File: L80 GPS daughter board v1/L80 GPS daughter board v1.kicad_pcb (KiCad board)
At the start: 2 copper layers, 29.8 x 18 mm, 12 parts, among them J1 Conn_01x06_Socket, U1 AP2112K-3.3, U2 L80-R, U3 MCP73831-2-OT

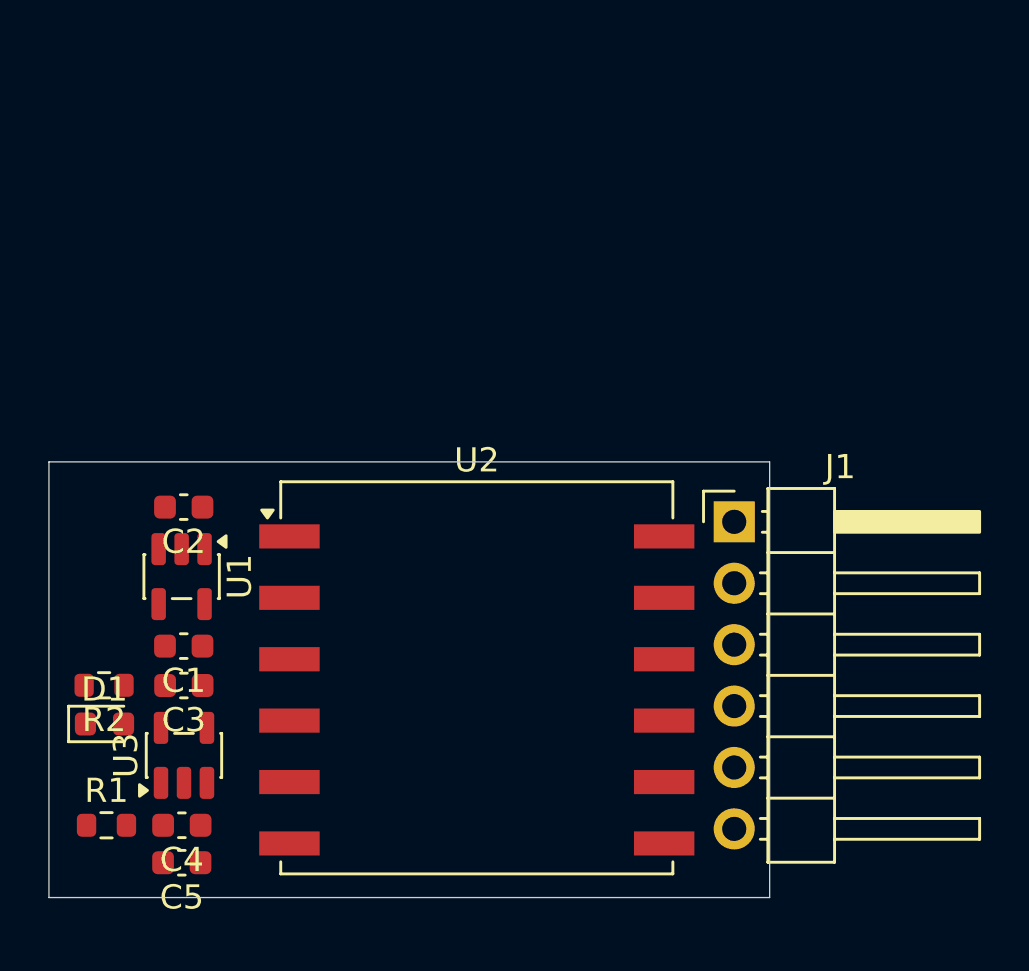
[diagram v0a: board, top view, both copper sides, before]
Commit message: started working on the L80 GPS carrier board
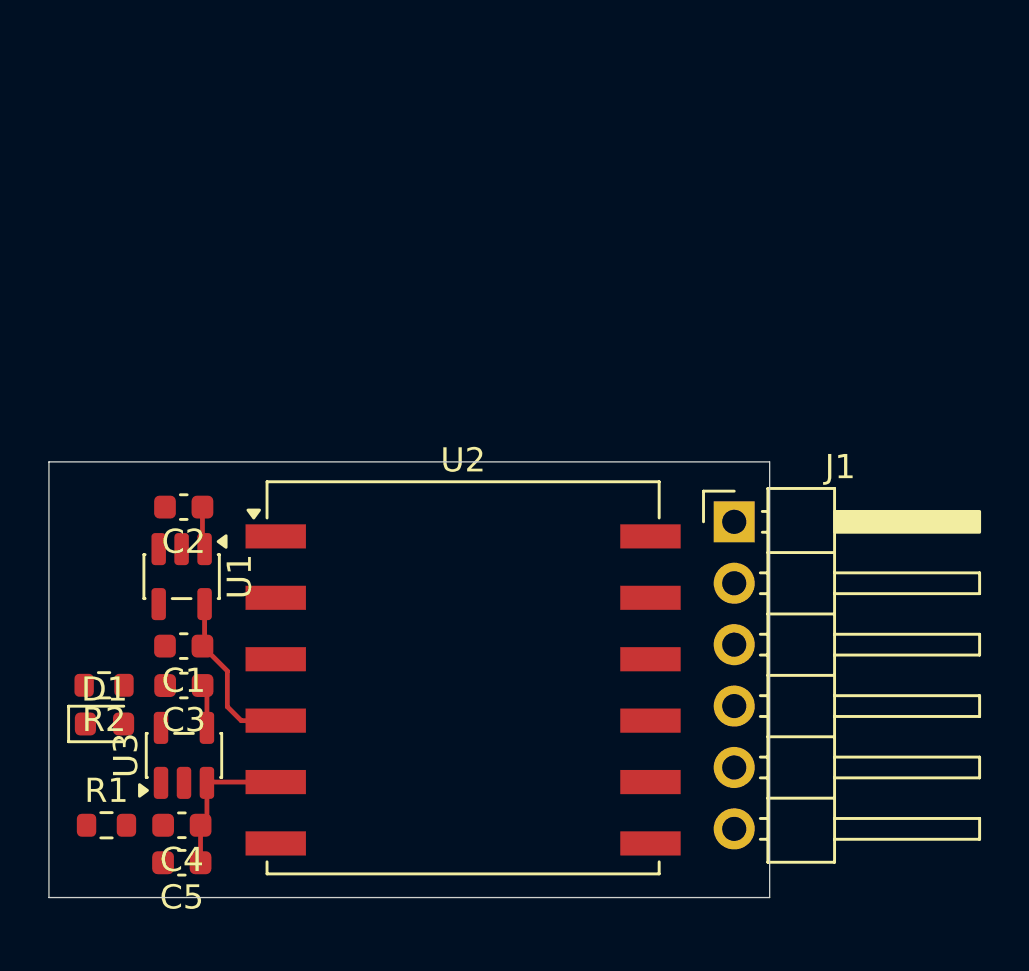
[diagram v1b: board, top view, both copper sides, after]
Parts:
- moved U2 0.57 mm to (134.2, 106.8)
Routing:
- net GPS_PWR: track 0.00 -> 6.95 mm
- net VBAT_RTC: track 0.00 -> 6.27 mm
- net +5V: track 0.00 -> 3.60 mm
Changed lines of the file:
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@@
 	(footprint "RF_GPS:Quectel_L80-R"
 		(layer "F.Cu")
-		(at 134.817089 106.801883)
+		(at 134.25 106.801883)
 		(descr "Quectel L80-R GPS Module, Patch on Top, https://www.quectel.com/UploadImage/Downlad/Quectel_L80-R_Hardware_Design_V1.2.pdf")
 		(tags "quectel GPS GNSS")
@@
 			(polygon
 				(pts
-					(xy 135.471864 106.171883) (xy 135.452801 105.953994) (xy 135.396192 105.742725) (xy 135.303756 105.544496)
-					(xy 135.178302 105.365329) (xy 135.023643 105.21067) (xy 134.844477 105.085216) (xy 134.646247 104.99278)
-					(xy 134.434978 104.936171) (xy 134.217089 104.917108) (xy 133.9992 104.936171) (xy 133.787931 104.99278)
-					(xy 133.589702 105.085216) (xy 133.410535 105.21067) (xy 133.255876 105.365329) (xy 133.130422 105.544496)
-					(xy 133.037986 105.742725) (xy 132.981377 105.953994) (xy 132.962314 106.171883) (xy 132.981377 106.389772)
-					(xy 133.037986 106.601041) (xy 133.130422 106.79927) (xy 133.255876 106.978437) (xy 133.410535 107.133096)
-					(xy 133.589701 107.25855) (xy 133.787931 107.350986) (xy 133.9992 107.407595) (xy 134.217089 107.426658)
-					(xy 134.434978 107.407595) (xy 134.646247 107.350986) (xy 134.844477 107.25855) (xy 135.023643 107.133096)
-					(xy 135.178302 106.978437) (xy 135.303756 106.79927) (xy 135.396192 106.601041) (xy 135.452801 106.389772)
+					(xy 134.904775 106.171883) (xy 134.885712 105.953994) (xy 134.829103 105.742725) (xy 134.736667 105.544496)
+					(xy 134.611213 105.365329) (xy 134.456554 105.21067) (xy 134.277388 105.085216) (xy 134.079158 104.99278)
+					(xy 133.867889 104.936171) (xy 133.65 104.917108) (xy 133.432111 104.936171) (xy 133.220842 104.99278)
+					(xy 133.022613 105.085216) (xy 132.843446 105.21067) (xy 132.688787 105.365329) (xy 132.563333 105.544496)
+					(xy 132.470897 105.742725) (xy 132.414288 105.953994) (xy 132.395225 106.171883) (xy 132.414288 106.389772)
+					(xy 132.470897 106.601041) (xy 132.563333 106.79927) (xy 132.688787 106.978437) (xy 132.843446 107.133096)
+					(xy 133.022612 107.25855) (xy 133.220842 107.350986) (xy 133.432111 107.407595) (xy 133.65 107.426658)
+					(xy 133.867889 107.407595) (xy 134.079158 107.350986) (xy 134.277388 107.25855) (xy 134.456554 107.133096)
+					(xy 134.611213 106.978437) (xy 134.736667 106.79927) (xy 134.829103 106.601041) (xy 134.885712 106.389772)
 				)
 			)
@@
 		(layer "Edge.Cuts")
 	)
+	(segment
+		(start 123.5575 105.4025)
+		(end 123.47 105.49)
+		(width 0.2)
+		(layer "F.Cu")
+		(net 2)
+	)
+	(segment
+		(start 126.5 108.571883)
+		(end 125.071883 108.571883)
+		(width 0.2)
+		(layer "F.Cu")
+		(net 2)
+	)
+	(segment
+		(start 125.071883 108.571883)
+		(end 124.5 108)
+		(width 0.2)
+		(layer "F.Cu")
+		(net 2)
+	)
+	(segment
+		(start 123.5575 103.7525)
+		(end 123.5575 105.4025)
+		(width 0.2)
+		(layer "F.Cu")
+		(net 2)
+	)
+	(segment
+		(start 124.5 106.52)
+		(end 124.5 108)
+		(width 0.2)
+		(layer "F.Cu")
+		(net 2)
+	)
+	(segment
+		(start 123.47 105.49)
+		(end 124.5 106.52)
+		(width 0.2)
+		(layer "F.Cu")
+		(net 2)
+	)
+	(segment
+		(start 123.655 107.3)
+		(end 123.475 107.12)
+		(width 0.2)
+		(layer "F.Cu")
+		(net 3)
+	)
+	(segment
+		(start 123.47 101.39)
+		(end 123.5575 101.4775)
+		(width 0.2)
+		(layer "F.Cu")
+		(net 3)
+	)
+	(segment
+		(start 123.655 108.8725)
+		(end 123.655 107.3)
+		(width 0.2)
+		(layer "F.Cu")
+		(net 3)
+	)
+	(segment
+		(start 123.47 99.74)
+		(end 123.47 101.39)
+		(width 0.2)
+		(layer "F.Cu")
+		(net 3)
+	)
+	(segment
+		(start 123.655 111.1475)
+		(end 123.655 112.6375)
+		(width 0.2)
+		(layer "F.Cu")
+		(net 14)
+	)
+	(segment
+		(start 123.39 112.9025)
+		(end 123.3925 112.9)
+		(width 0.2)
+		(layer "F.Cu")
+		(net 14)
+	)
+	(segment
+		(start 123.39 114.45)
+		(end 123.39 112.9025)
+		(width 0.2)
+		(layer "F.Cu")
+		(net 14)
+	)
+	(segment
+		(start 123.655 112.6375)
+		(end 123.3925 112.9)
+		(width 0.2)
+		(layer "F.Cu")
+		(net 14)
+	)
+	(segment
+		(start 123.690617 111.111883)
+		(end 123.655 111.1475)
+		(width 0.2)
+		(layer "F.Cu")
+		(net 14)
+	)
+	(segment
+		(start 126.5 111.111883)
+		(end 123.690617 111.111883)
+		(width 0.2)
+		(layer "F.Cu")
+		(net 14)
+	)
 	(embedded_fonts no)

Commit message: routed the l80 gps daughter board and a few more modifications
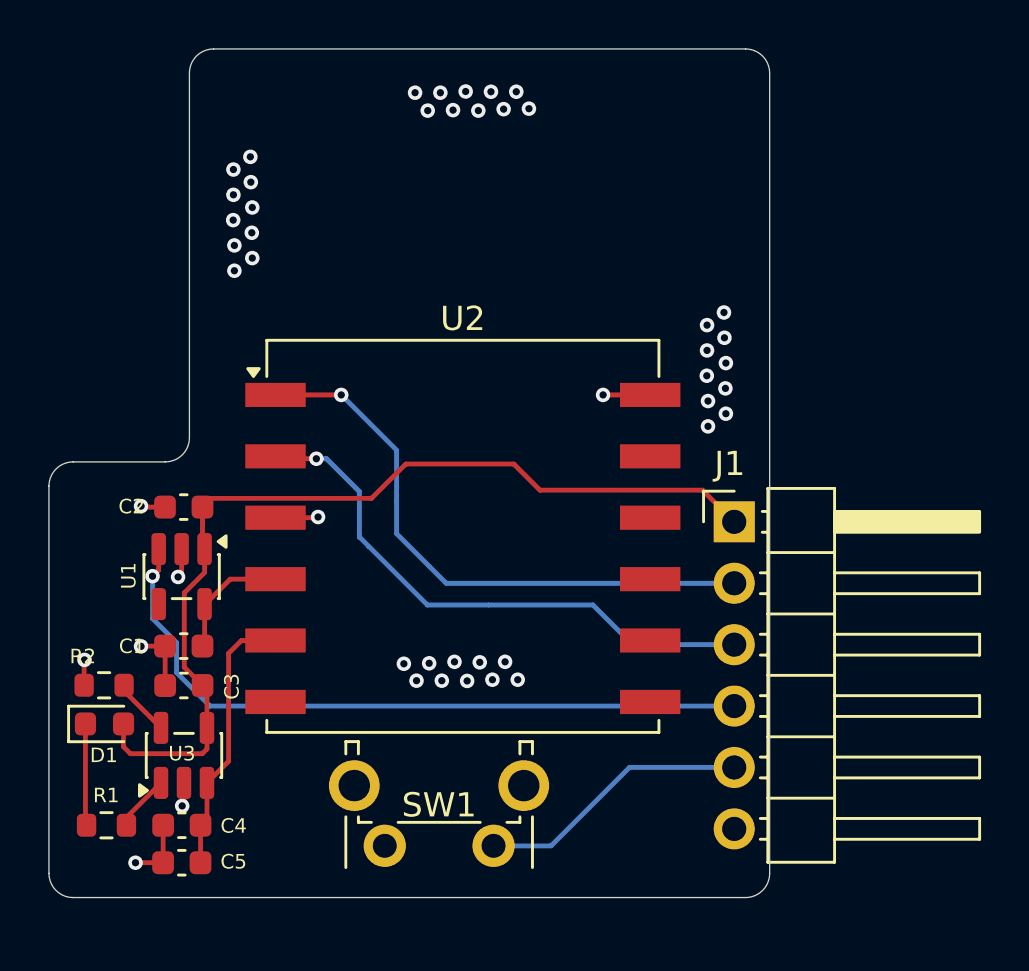
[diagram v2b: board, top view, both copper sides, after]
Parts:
- added SW1: SW_Push, Button_Switch_THT:SW_Tactile_SPST_Angled_PTS645Vx39-2LFS, F.Cu at (135.5, 113.8)
- moved U2 5.85 mm to (134.2, 101.0)
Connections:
- J1 pad 5: unconnected-(J1-Pin_5-Pad5) -> PWR_SWITCH
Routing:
- net +5V: track 3.60 -> 39.1 mm
- net GPS_Switch: track 0.00 -> 29.3 mm, vias 0 -> 1
- net gps_rx: track 0.00 -> 24.2 mm, vias 0 -> 1
- net gps_tx: track 0.00 -> 23.3 mm, vias 0 -> 1
- net GND: track 0.00 -> 13.3 mm, vias 0 -> 48
- net PWR_SWITCH: track 0.00 -> 11.3 mm
- net VBAT_RTC: track 6.27 -> 11.3 mm
- net Net-(D1-K): track 0.00 -> 4.21 mm
- net Net-(U3-PROG): track 0.00 -> 2.40 mm
- net stat: track 0.00 -> 2.34 mm
- net GPS_PWR: track 6.95 -> 5.13 mm
- added copper zone on In1.Cu, net GND
- added copper zone on In2.Cu, net GND
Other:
- board size 29.8 x 18 mm -> 29.8 x 35.1 mm
- copper layers 2 -> 4

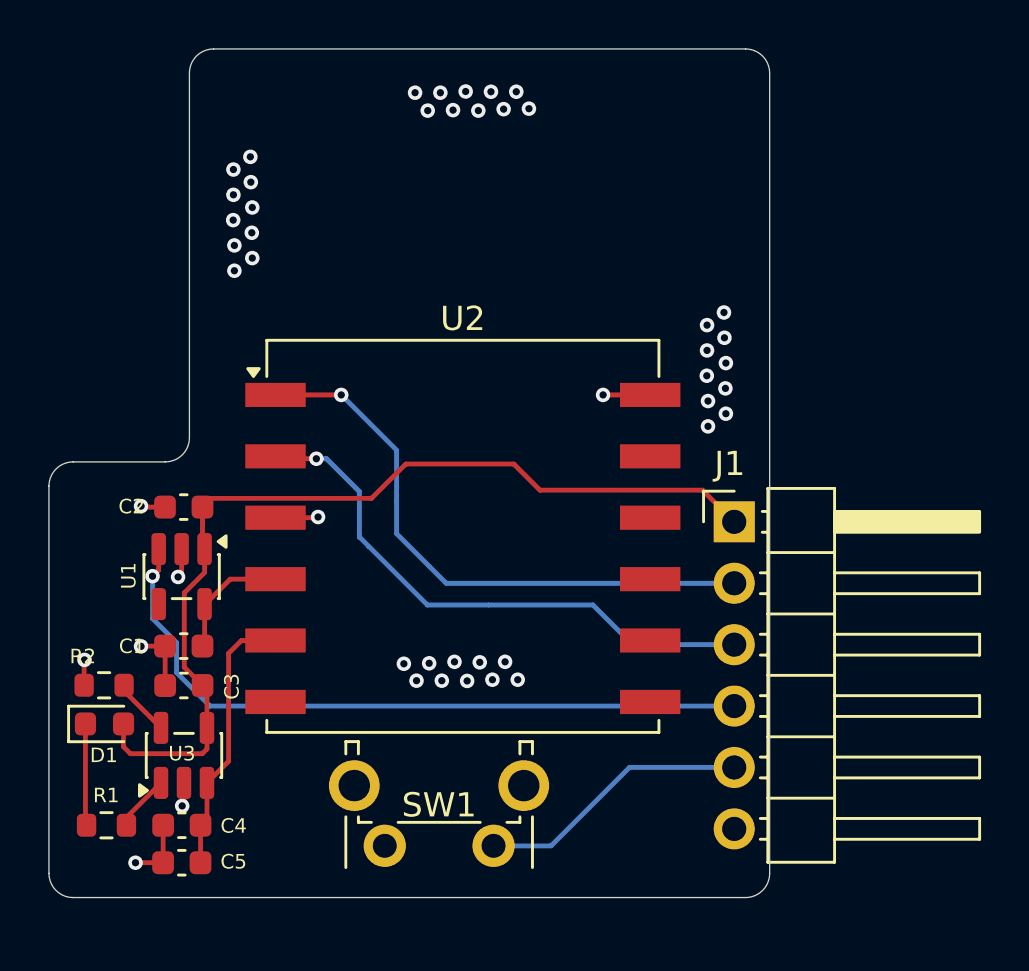
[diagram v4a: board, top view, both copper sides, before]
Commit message: started on the enclosure designs
started on the enclosure designs
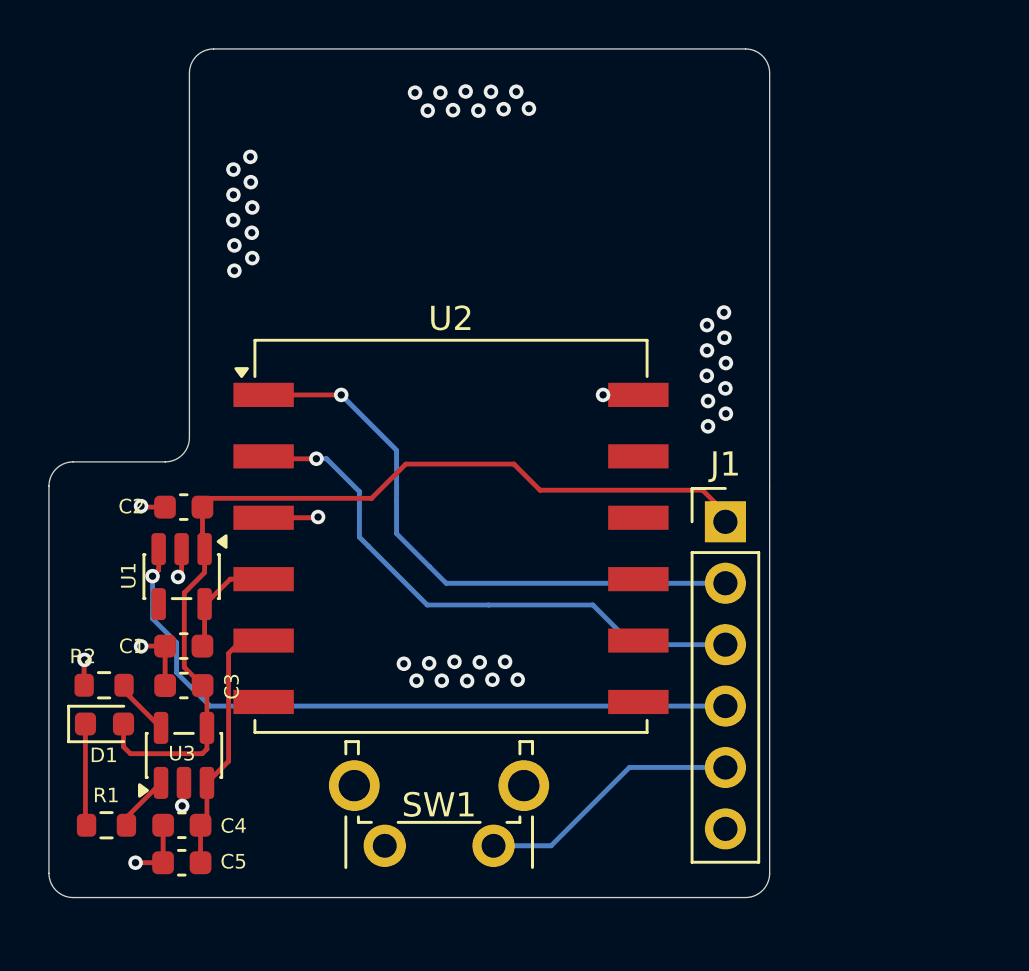
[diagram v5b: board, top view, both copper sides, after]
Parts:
- J1: footprint Connector_PinHeader_2.54mm:PinHeader_1x06_P2.54mm_Horizontal -> Connector_PinHeader_2.54mm:PinHeader_1x06_P2.54mm_Vertical
- moved U2 0.49 mm to (133.8, 101.0)
- moved J1 0.37 mm to (145.1, 100.3)
